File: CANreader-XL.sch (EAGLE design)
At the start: 99 parts, among them IC1 STM32F107RBT, IC2 TJA1055T/3, IC3 BD9G101G, IC4 LM1117IMPX-3.3, IC5 MCP2562-SOIC8, IC7 DP83848I, Q1 25MHz, SW1 SLEEP, SW2 TERM, U1 HC_05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

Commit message: Test inital routing
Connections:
- removed net N$29: J1.TD-
- net TD-: now also J1.TD-
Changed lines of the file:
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@@
 <pinref part="R25" gate="G$1" pin="1"/>
 <wire x1="160.02" y1="-129.54" x2="160.02" y2="-127" width="0.1524" layer="91"/>
-<wire x1="160.02" y1="-127" x2="148.59" y2="-127" width="0.1524" layer="91"/>
-<label x="148.59" y="-127" size="1.778" layer="95" rot="R180" xref="yes"/>
+<label x="151.13" y="-127" size="1.778" layer="95" rot="R180" xref="yes"/>
+<wire x1="152.4" y1="-127" x2="151.13" y2="-127" width="0.1524" layer="91"/>
+<wire x1="160.02" y1="-127" x2="203.2" y2="-127" width="0.1524" layer="91"/>
+<pinref part="J1" gate="G$1" pin="TD-"/>
+<wire x1="152.4" y1="-127" x2="160.02" y2="-127" width="0.1524" layer="91"/>
+<junction x="160.02" y="-127"/>
 </segment>
 </net>
@@
 </segment>
 </net>
-<net name="N$29" class="0">
-<segment>
-<wire x1="160.02" y1="-127" x2="203.2" y2="-127" width="0.1524" layer="91"/>
-<pinref part="J1" gate="G$1" pin="TD-"/>
-</segment>
-</net>

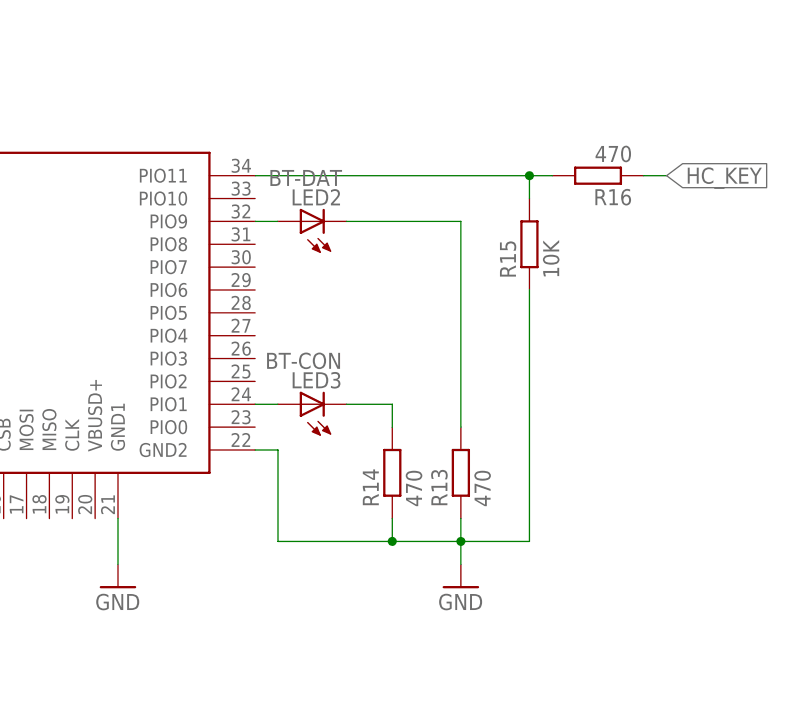
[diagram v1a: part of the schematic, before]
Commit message: Fix BT LED
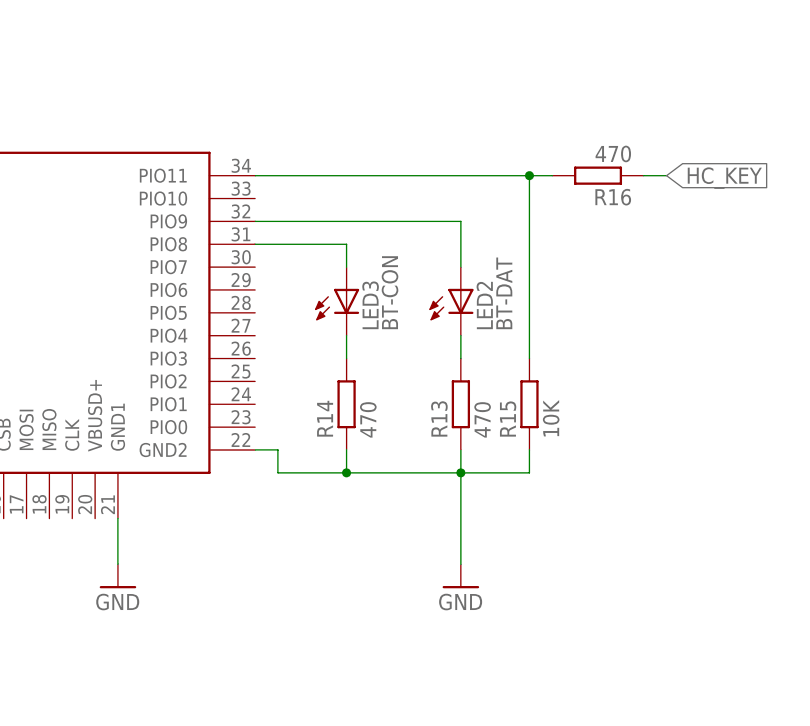
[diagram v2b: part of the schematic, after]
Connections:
- removed net N$15: LED3.A, U1.PIO1
- new net N$5: LED3.A, U1.PIO8
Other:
- moved on the sheet: LED2, LED3, R13, R14, R15
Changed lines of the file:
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@@
 <instance part="C25" gate="G$1" x="170.18" y="-33.02"/>
 <instance part="+3V5" gate="G$1" x="180.34" y="-7.62"/>
-<instance part="R13" gate="G$1" x="264.16" y="-33.02" rot="R90"/>
-<instance part="R14" gate="G$1" x="256.54" y="-33.02" rot="R90"/>
-<instance part="R15" gate="G$1" x="271.78" y="-7.62" rot="R90"/>
+<instance part="R13" gate="G$1" x="264.16" y="-25.4" rot="R90"/>
+<instance part="R14" gate="G$1" x="251.46" y="-25.4" rot="R90"/>
+<instance part="R15" gate="G$1" x="271.78" y="-25.4" rot="R90"/>
 <instance part="R16" gate="G$1" x="279.4" y="0" rot="R180"/>
 <instance part="R17" gate="G$1" x="180.34" y="-17.78" rot="R270"/>
@@
 <instance part="GND31" gate="1" x="93.98" y="-83.82"/>
 <instance part="R22" gate="G$1" x="-43.18" y="-106.68" rot="R270"/>
-<instance part="LED2" gate="G$1" x="246.38" y="-5.08" rot="R90"/>
-<instance part="LED3" gate="G$1" x="246.38" y="-25.4" rot="R90"/>
+<instance part="LED2" gate="G$1" x="264.16" y="-12.7"/>
+<instance part="LED3" gate="G$1" x="251.46" y="-12.7"/>
 <instance part="LED1" gate="G$1" x="149.86" y="17.78" rot="R90"/>
 <instance part="SW2" gate="G$1" x="-55.88" y="-104.14"/>
@@
 <pinref part="U1" gate="G$1" pin="GND2"/>
 <wire x1="243.84" y1="-30.48" x2="241.3" y2="-30.48" width="0.1524" layer="91"/>
-<wire x1="243.84" y1="-40.64" x2="243.84" y2="-30.48" width="0.1524" layer="91"/>
+<wire x1="243.84" y1="-33.02" x2="243.84" y2="-30.48" width="0.1524" layer="91"/>
 <pinref part="R15" gate="G$1" pin="1"/>
-<wire x1="264.16" y1="-40.64" x2="256.54" y2="-40.64" width="0.1524" layer="91"/>
-<wire x1="256.54" y1="-40.64" x2="243.84" y2="-40.64" width="0.1524" layer="91"/>
-<wire x1="271.78" y1="-12.7" x2="271.78" y2="-40.64" width="0.1524" layer="91"/>
-<wire x1="271.78" y1="-40.64" x2="264.16" y2="-40.64" width="0.1524" layer="91"/>
+<wire x1="264.16" y1="-33.02" x2="251.46" y2="-33.02" width="0.1524" layer="91"/>
+<wire x1="251.46" y1="-33.02" x2="243.84" y2="-33.02" width="0.1524" layer="91"/>
+<wire x1="271.78" y1="-30.48" x2="271.78" y2="-33.02" width="0.1524" layer="91"/>
+<wire x1="271.78" y1="-33.02" x2="264.16" y2="-33.02" width="0.1524" layer="91"/>
 <pinref part="R13" gate="G$1" pin="1"/>
-<wire x1="264.16" y1="-38.1" x2="264.16" y2="-40.64" width="0.1524" layer="91"/>
-<junction x="264.16" y="-40.64"/>
+<wire x1="264.16" y1="-30.48" x2="264.16" y2="-33.02" width="0.1524" layer="91"/>
+<junction x="264.16" y="-33.02"/>
 <pinref part="R14" gate="G$1" pin="1"/>
-<wire x1="256.54" y1="-38.1" x2="256.54" y2="-40.64" width="0.1524" layer="91"/>
-<junction x="256.54" y="-40.64"/>
+<wire x1="251.46" y1="-30.48" x2="251.46" y2="-33.02" width="0.1524" layer="91"/>
+<junction x="251.46" y="-33.02"/>
 <pinref part="GND34" gate="1" pin="GND"/>
-<wire x1="264.16" y1="-40.64" x2="264.16" y2="-43.18" width="0.1524" layer="91"/>
+<wire x1="264.16" y1="-33.02" x2="264.16" y2="-43.18" width="0.1524" layer="91"/>
 </segment>
 <segment>
@@
 <pinref part="R15" gate="G$1" pin="2"/>
 <wire x1="241.3" y1="0" x2="271.78" y2="0" width="0.1524" layer="91"/>
-<wire x1="271.78" y1="0" x2="271.78" y2="-2.54" width="0.1524" layer="91"/>
+<wire x1="271.78" y1="0" x2="271.78" y2="-20.32" width="0.1524" layer="91"/>
 <pinref part="R16" gate="G$1" pin="2"/>
 <wire x1="271.78" y1="0" x2="274.32" y2="0" width="0.1524" layer="91"/>
@@
 </segment>
 </net>
-<net name="N$10" class="0">
-<segment>
-<pinref part="U1" gate="G$1" pin="PIO9"/>
-<pinref part="LED2" gate="G$1" pin="A"/>
-<wire x1="241.3" y1="-5.08" x2="243.84" y2="-5.08" width="0.1524" layer="91"/>
-</segment>
-</net>
 <net name="N$11" class="0">
 <segment>
 <pinref part="LED2" gate="G$1" pin="C"/>
 <pinref part="R13" gate="G$1" pin="2"/>
-<wire x1="251.46" y1="-5.08" x2="264.16" y2="-5.08" width="0.1524" layer="91"/>
-<wire x1="264.16" y1="-5.08" x2="264.16" y2="-27.94" width="0.1524" layer="91"/>
-</segment>
-</net>
-<net name="N$15" class="0">
-<segment>
-<pinref part="LED3" gate="G$1" pin="A"/>
-<pinref part="U1" gate="G$1" pin="PIO1"/>
-<wire x1="243.84" y1="-25.4" x2="241.3" y2="-25.4" width="0.1524" layer="91"/>
+<wire x1="264.16" y1="-17.78" x2="264.16" y2="-20.32" width="0.1524" layer="91"/>
 </segment>
 </net>
@@
 <pinref part="LED3" gate="G$1" pin="C"/>
 <pinref part="R14" gate="G$1" pin="2"/>
-<wire x1="251.46" y1="-25.4" x2="256.54" y2="-25.4" width="0.1524" layer="91"/>
-<wire x1="256.54" y1="-25.4" x2="256.54" y2="-27.94" width="0.1524" layer="91"/>
+<wire x1="251.46" y1="-17.78" x2="251.46" y2="-20.32" width="0.1524" layer="91"/>
 </segment>
 </net>
@@
 </segment>
 </net>
+<net name="N$5" class="0">
+<segment>
+<pinref part="LED3" gate="G$1" pin="A"/>
+<wire x1="251.46" y1="-10.16" x2="251.46" y2="-7.62" width="0.1524" layer="91"/>
+<pinref part="U1" gate="G$1" pin="PIO8"/>
+<wire x1="251.46" y1="-7.62" x2="241.3" y2="-7.62" width="0.1524" layer="91"/>
+</segment>
+</net>
+<net name="N$10" class="0">
+<segment>
+<pinref part="U1" gate="G$1" pin="PIO9"/>
+<wire x1="241.3" y1="-5.08" x2="264.16" y2="-5.08" width="0.1524" layer="91"/>
+<pinref part="LED2" gate="G$1" pin="A"/>
+<wire x1="264.16" y1="-5.08" x2="264.16" y2="-10.16" width="0.1524" layer="91"/>
+</segment>
+</net>

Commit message: BOOT selection
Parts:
- removed R9: 10K, rcl:R-EU_R0805
- added JP1: BOOT, pinhead:PINHD-1X3
- added R6: 10K, rcl:R-EU_R0805
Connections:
- new net N$29: JP1.2, R6.1
- net +3V3: now also JP1.3
- net GND: now also JP1.1; no longer R9.1
- net N$3: now also R6.2; no longer R9.2
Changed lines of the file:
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@@
 <part name="C24" library="rcl" deviceset="C-EU" device="C0805" value="4.7uF"/>
 <part name="GND14" library="supply1" deviceset="GND" device=""/>
-<part name="R9" library="rcl" deviceset="R-EU_" device="R0805" value="10K"/>
 <part name="GND15" library="supply1" deviceset="GND" device=""/>
 <part name="R10" library="rcl" deviceset="R-EU_" device="R0805" value="10K"/>
@@
 <part name="C40" library="rcl" deviceset="C-EU" device="C0805" value="0.1uF"/>
 <part name="GND12" library="supply1" deviceset="GND" device=""/>
+<part name="JP1" library="pinhead" deviceset="PINHD-1X3" device="" value="BOOT"/>
+<part name="+3V7" library="supply1" deviceset="+3V3" device=""/>
+<part name="R6" library="rcl" deviceset="R-EU_" device="R0805" value="10K"/>
 </parts>
 <sheets>
@@
 <instance part="C24" gate="G$1" x="58.42" y="177.8"/>
 <instance part="GND14" gate="1" x="-83.82" y="50.8"/>
-<instance part="R9" gate="G$1" x="48.26" y="-10.16" rot="R90"/>
 <instance part="GND15" gate="1" x="147.32" y="40.64"/>
 <instance part="R10" gate="G$1" x="139.7" y="45.72"/>
-<instance part="GND16" gate="1" x="48.26" y="-20.32"/>
+<instance part="GND16" gate="1" x="7.62" y="-12.7"/>
 <instance part="GND17" gate="1" x="-33.02" y="-12.7"/>
 <instance part="D4" gate="D$1" x="-40.64" y="71.12" rot="R90"/>
@@
 <instance part="C40" gate="G$1" x="-12.7" y="-66.04" rot="R180"/>
 <instance part="GND12" gate="1" x="-12.7" y="-73.66"/>
+<instance part="JP1" gate="A" x="-5.08" y="-2.54" rot="R180"/>
+<instance part="+3V7" gate="G$1" x="7.62" y="7.62"/>
+<instance part="R6" gate="G$1" x="17.78" y="-2.54"/>
 </instances>
 <busses>
@@
 <segment>
 <pinref part="GND16" gate="1" pin="GND"/>
-<wire x1="48.26" y1="-15.24" x2="48.26" y2="-17.78" width="0.1524" layer="91"/>
-<pinref part="R9" gate="G$1" pin="1"/>
+<pinref part="JP1" gate="A" pin="1"/>
+<wire x1="-2.54" y1="-5.08" x2="7.62" y2="-5.08" width="0.1524" layer="91"/>
+<wire x1="7.62" y1="-5.08" x2="7.62" y2="-10.16" width="0.1524" layer="91"/>
 </segment>
 <segment>
@@
 <junction x="-12.7" y="-55.88"/>
 </segment>
+<segment>
+<pinref part="JP1" gate="A" pin="3"/>
+<wire x1="-2.54" y1="0" x2="7.62" y2="0" width="0.1524" layer="91"/>
+<pinref part="+3V7" gate="G$1" pin="+3V3"/>
+<wire x1="7.62" y1="5.08" x2="7.62" y2="0" width="0.1524" layer="91"/>
+</segment>
 </net>
 <net name="CAN1_RX" class="0">
@@
 </segment>
 </net>
-<net name="N$3" class="0">
-<segment>
-<pinref part="R9" gate="G$1" pin="2"/>
-<wire x1="48.26" y1="-2.54" x2="48.26" y2="-5.08" width="0.1524" layer="91"/>
-<pinref part="IC1" gate="MCU" pin="BOOT0"/>
-<wire x1="50.8" y1="-2.54" x2="48.26" y2="-2.54" width="0.1524" layer="91"/>
-</segment>
-</net>
 <net name="N$25" class="0">
 <segment>
@@
 </segment>
 </net>
+<net name="N$3" class="0">
+<segment>
+<pinref part="IC1" gate="MCU" pin="BOOT0"/>
+<pinref part="R6" gate="G$1" pin="2"/>
+<wire x1="50.8" y1="-2.54" x2="22.86" y2="-2.54" width="0.1524" layer="91"/>
+</segment>
+</net>
+<net name="N$29" class="0">
+<segment>
+<pinref part="R6" gate="G$1" pin="1"/>
+<pinref part="JP1" gate="A" pin="2"/>
+<wire x1="12.7" y1="-2.54" x2="-2.54" y2="-2.54" width="0.1524" layer="91"/>
+</segment>
+</net>
